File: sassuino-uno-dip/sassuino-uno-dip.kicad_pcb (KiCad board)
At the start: 2 copper layers, 68.6 x 53.3 mm, 31 parts, among them J1 USB_B, J10 OSCPWR_HDR, J2 POWER2_HDR, J3 ICSP_HDR, J4 POWER_HDR, J5 PORTC_HDR, J6 PORTB_HDR, J7 PORTD_HDR, J8 XTAL2_HDR, J9 XTAL1_HDR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

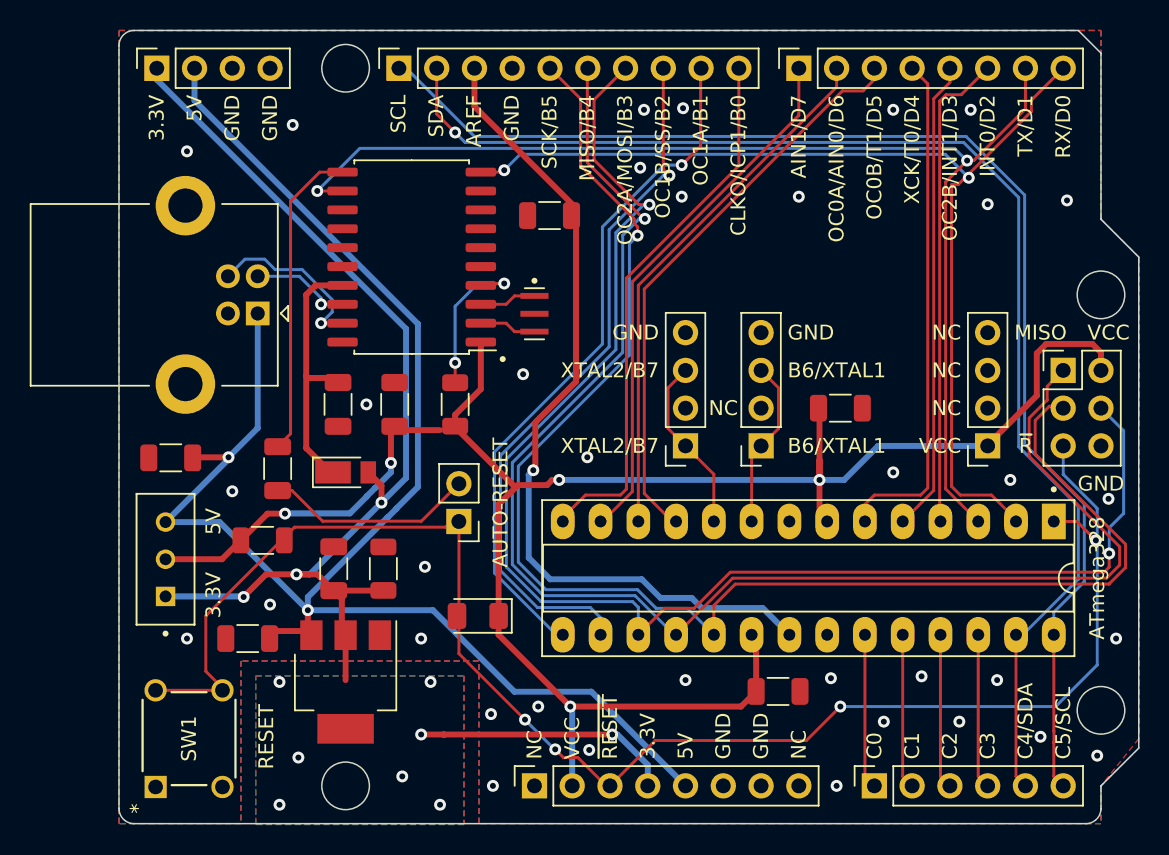
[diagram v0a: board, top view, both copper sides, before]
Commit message: Move decoupling capacitors closer to the IC pins.
Also connect the caps' ground pad directly to the IC ground pin,
rather than to the ground plane.
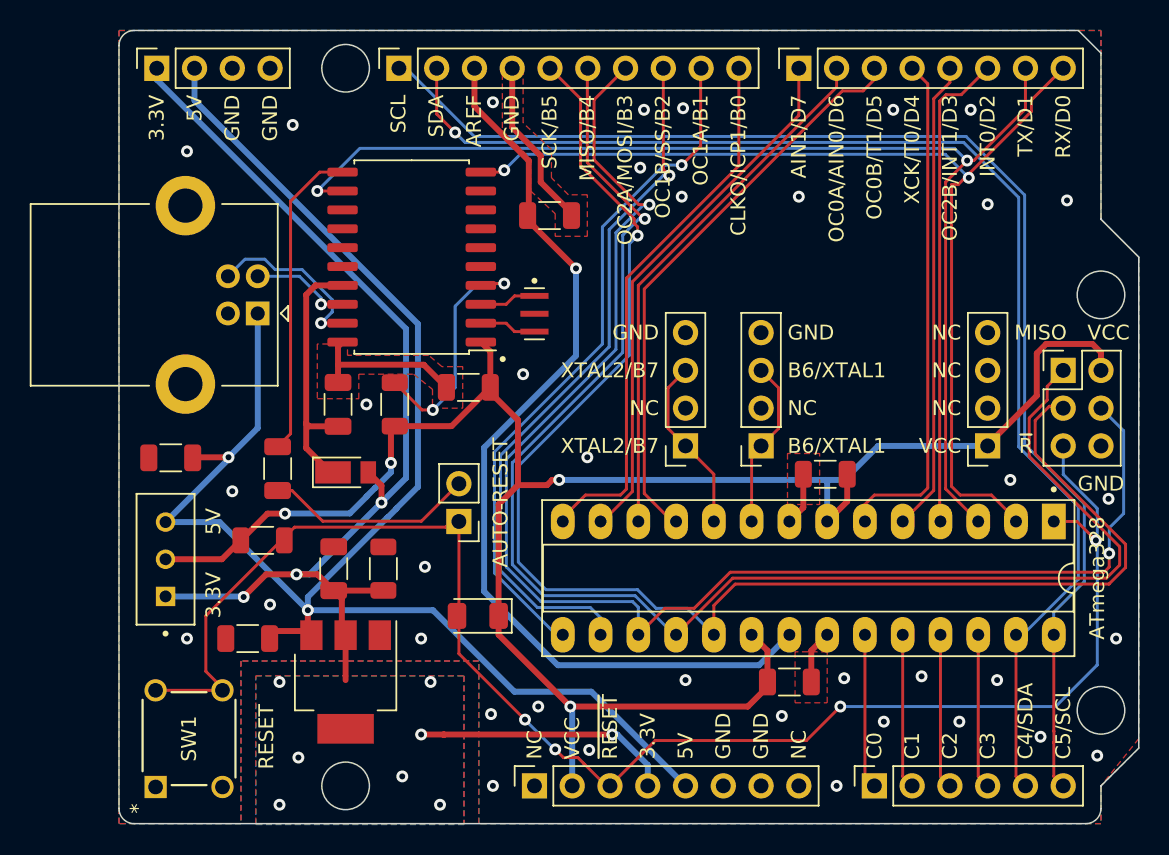
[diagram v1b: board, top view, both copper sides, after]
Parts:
- moved C9 5.08 mm to (74.3, 125.6), turned to 180 degrees
- moved C7 4.56 mm to (98.3, 131.4), turned to 0 degrees
- moved R3 4.06 mm to (69.3, 126.7)
- moved C8 0.99 mm to (95.9, 145.4)
- turned C1 to 0 degrees
- turned C3 to 90 degrees
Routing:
- net GND: track 0.00 -> 29.3 mm, vias 36 -> 37
- net /AREF: track 56.7 -> 64.0 mm
- net /~{RST}: track 10.5 -> 16.3 mm
- net VCC: track 129.3 -> 130.9 mm, vias 5 -> 4
- net /VUSB: track 18.2 -> 17.1 mm

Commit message: Move RESET# protection diode next to the MCU input pin.
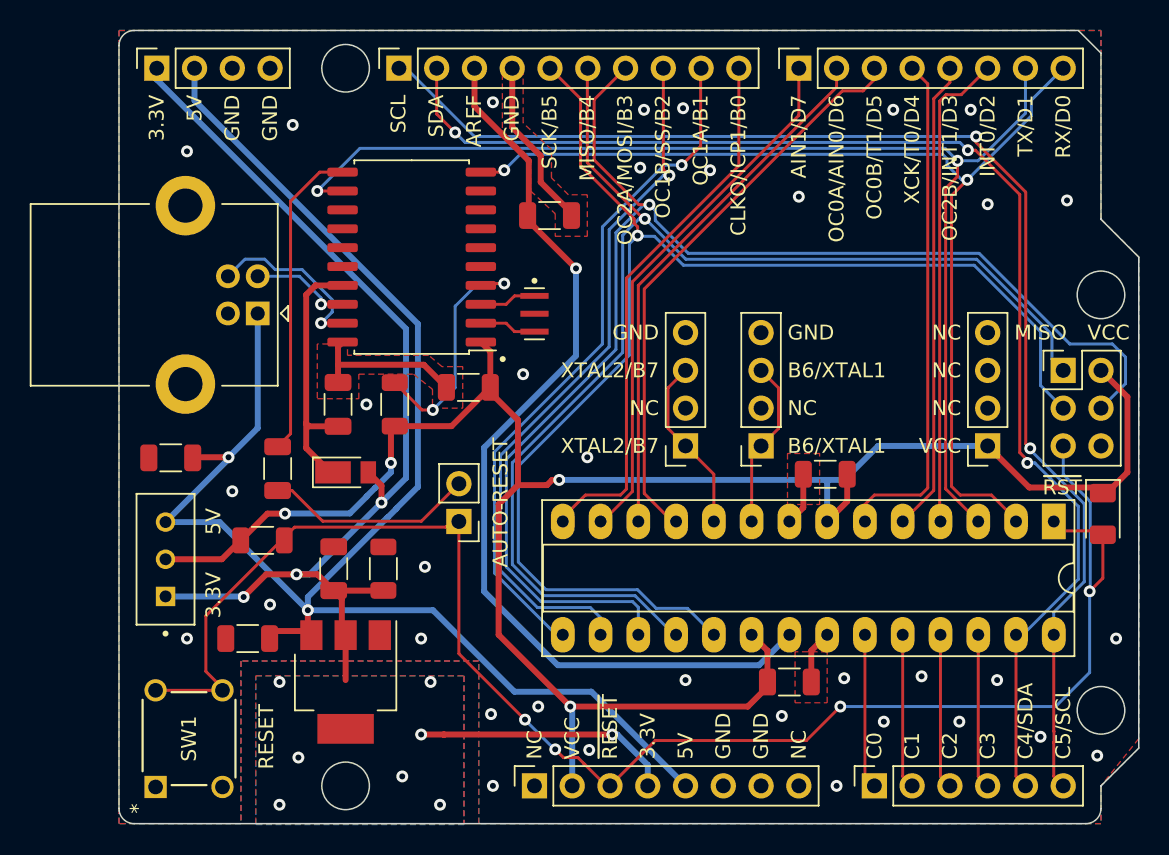
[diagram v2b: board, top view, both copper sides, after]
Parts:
- moved D2 42.6 mm to (117.0, 134.1), turned to -90 degrees
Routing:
- net /PB4/MISO: track 100.1 -> 85.1 mm
- net /PB5/SCK: track 99.4 -> 89.7 mm
- net VCC: track 130.9 -> 135.5 mm
- net /PB3/MOSI: track 97.1 -> 92.6 mm, vias 2 -> 1
- net /~{RESET}: track 107.2 -> 111.2 mm
- net /PC4/SDA: track 87.3 -> 87.8 mm, vias 1 -> 3
- net /PC5/SCL: track 87.6 -> 88.0 mm, vias 0 -> 2
- net GND: vias 37 -> 35
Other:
- board text added: "~{RST}"
- board text removed: "ATmega328"
- board text removed: "~{R}"

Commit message: Improve the reset circuit.
Add a 330R between the pushbutton reset switch and the capacitor, as
per the AVR hardware design doc.

Pull down the RTS# side of the capacitor with a 1K like in the Arduino
schematic.
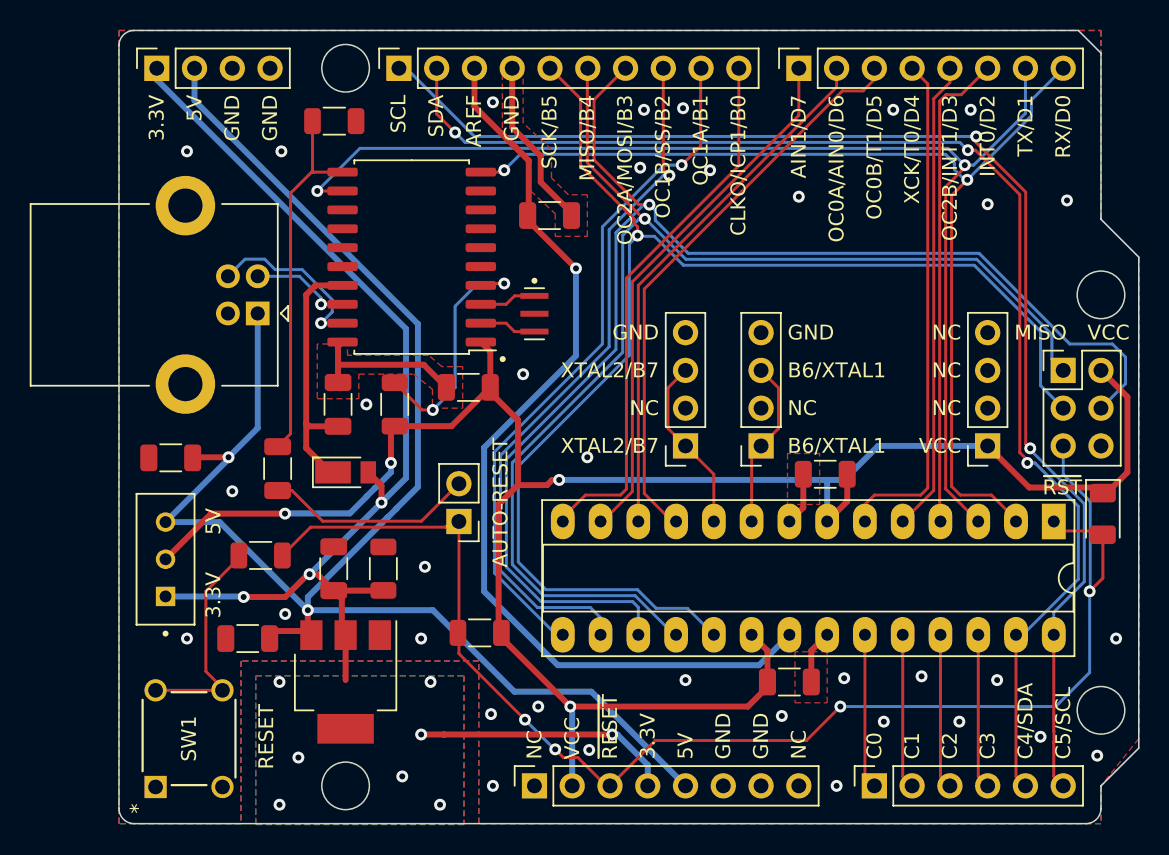
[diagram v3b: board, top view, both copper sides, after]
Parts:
- added R4: 1K, Resistor_SMD:R_1206_3216Metric, F.Cu at (65.3, 107.7)
- added R5: 330R, Resistor_SMD:R_1206_3216Metric, F.Cu at (60.3, 136.9)
- moved R1 15.9 mm to (75.1, 142.1), turned to 180 degrees
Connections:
- SW1 pad 2: /~{RESET} -> /RESET_SW
- SW1 pad 4: /~{RESET} -> /RESET_SW
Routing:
- net /~{RESET}: track 111.2 -> 93.2 mm
- net /RESET_SW: track 0.00 -> 14.7 mm
- net /~{RTS}: track 21.2 -> 24.9 mm
- net +3.3V: track 86.2 -> 85.3 mm

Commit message: Connect the Vin header pin.
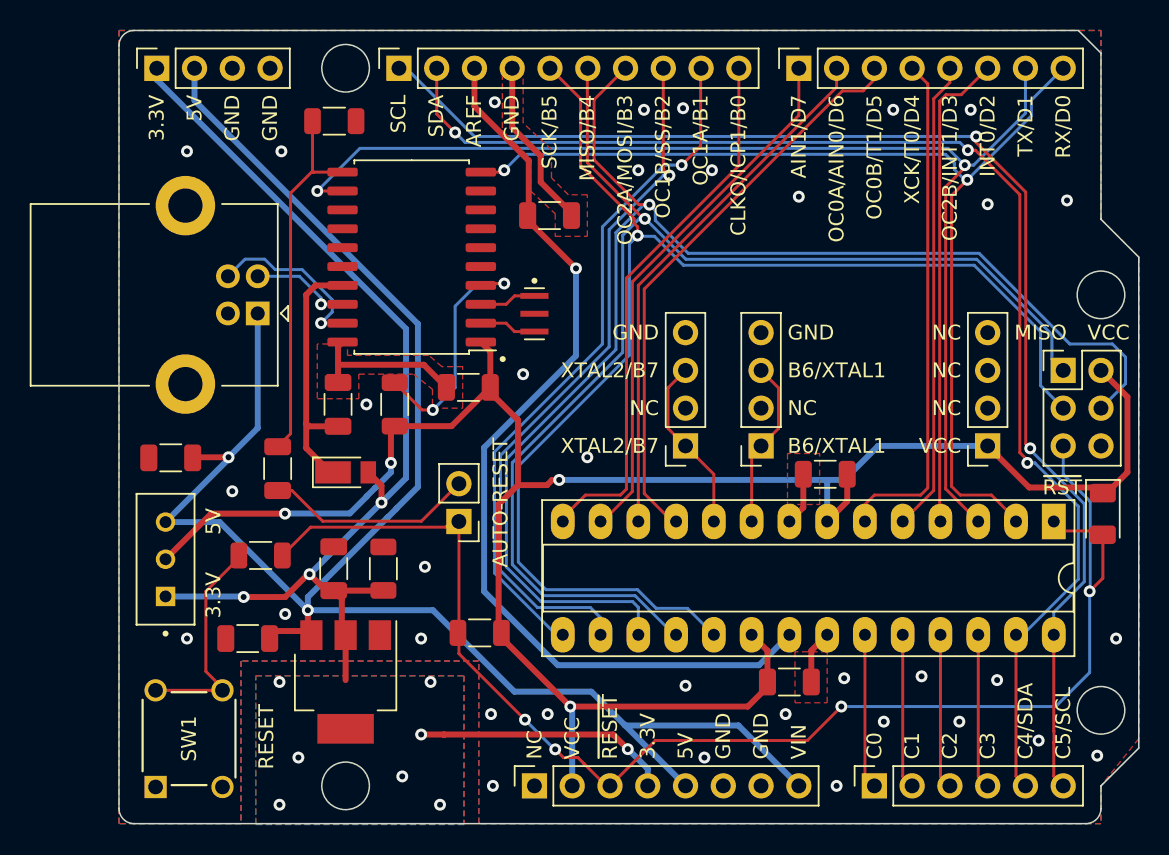
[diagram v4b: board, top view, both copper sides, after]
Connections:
- J4 pad 8: unconnected-(J4-Pad8) -> +5V
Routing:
- net +5V: track 110.7 -> 124.2 mm
- net +3.3V: track 85.3 -> 84.6 mm
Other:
- board text added: "VIN"

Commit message: Update to kicad 9
Various minor tweaks to PCB traces to satisfy the DRC.

Use a generic 3d model for the slide switch.
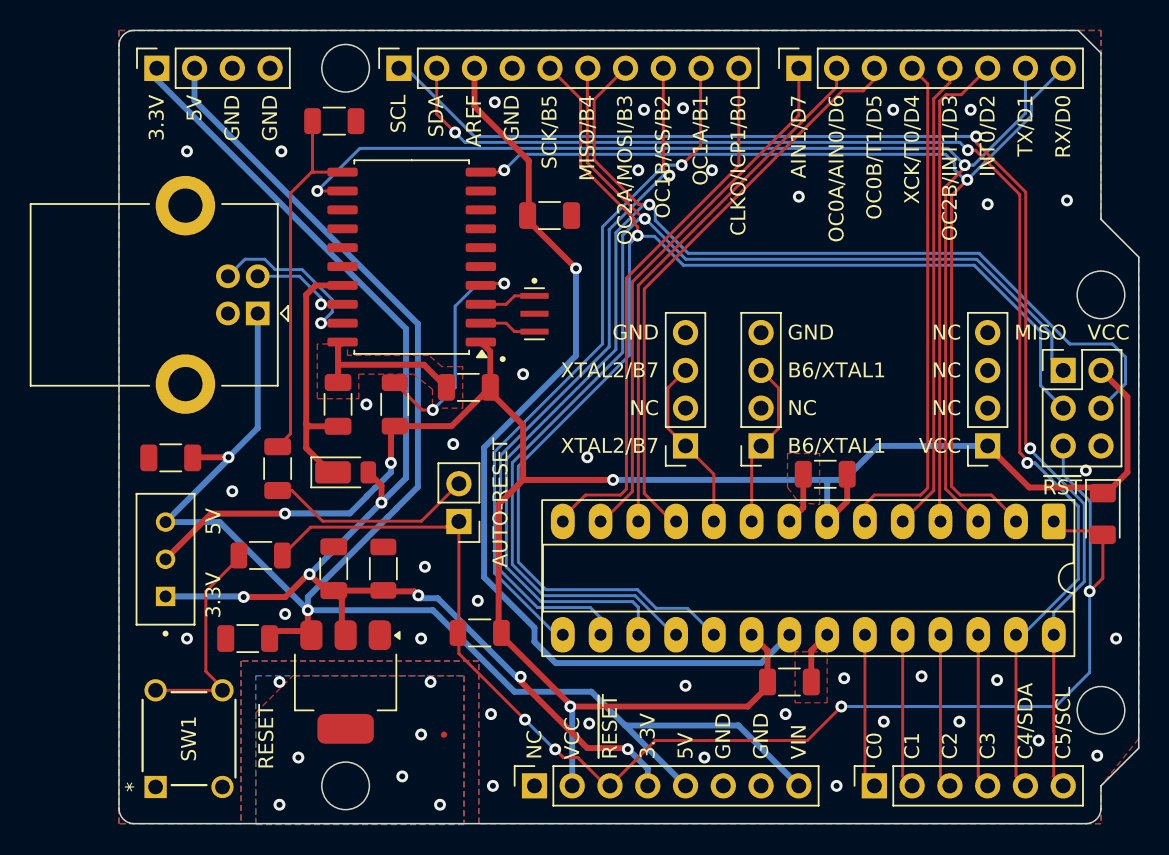
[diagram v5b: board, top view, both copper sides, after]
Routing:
- net GND: track 29.3 -> 17.9 mm, vias 35 -> 38
- net +3.3V: track 84.6 -> 88.4 mm, vias 11 -> 13

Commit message: Minor tweaks to PCB traces and copper fill zones.
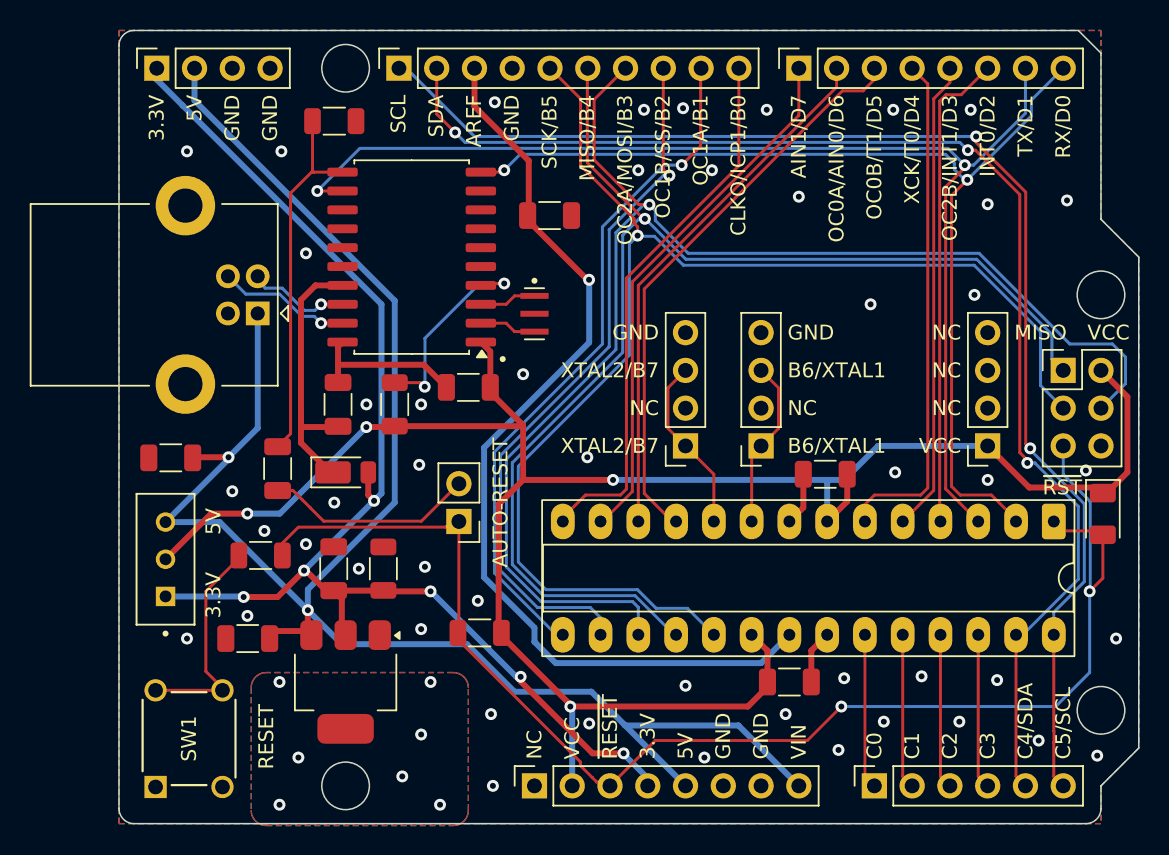
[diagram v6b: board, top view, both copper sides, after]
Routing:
- net /D+: track 12.0 -> 9.01 mm
- net /~{RST}: track 16.3 -> 13.7 mm
- net +3.3V: track 88.4 -> 85.9 mm
- net /VUSB: track 17.1 -> 18.5 mm
- net +5V: track 124.2 -> 122.9 mm
- net /AREF: track 63.9 -> 64.7 mm
- net /~{RESET}: vias 4 -> 2
- net GND: vias 38 -> 49
